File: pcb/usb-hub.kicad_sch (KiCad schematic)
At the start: 17 parts, among them U11 CH334P, Y2 X322512MSB4SI

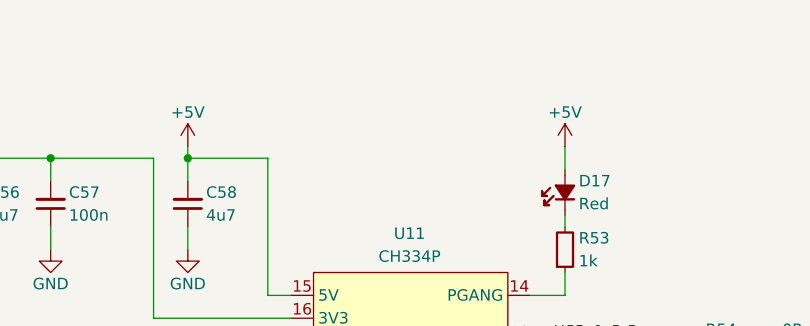
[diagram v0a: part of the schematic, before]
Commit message: [#5] Refactor the schematic
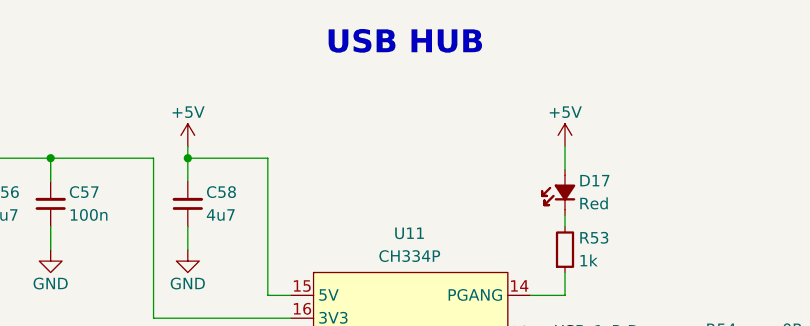
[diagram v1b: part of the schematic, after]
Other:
- note added: "USB HUB"
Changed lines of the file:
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@@
 		(comment 1 "Project author: Dominik Pluta")
+	)
+	(text "USB HUB"
+		(exclude_from_sim no)
+		(at 144.78 64.77 0)
+		(effects
+			(font
+				(size 2.54 2.54)
+				(bold yes)
+			)
+		)
 	)
 	(junction
